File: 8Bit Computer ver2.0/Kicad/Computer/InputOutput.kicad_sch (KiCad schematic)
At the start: 147 parts, among them IC102 SN74LVC1G32DBVR, IC236 SN74F521DWR, IC237 SN74F521DWR, IC238 DS1100Z-150+, IC239 SN74LVC1G14DBVR, IC240 SN74LVC1G86DBVR, IC241 SN74LVC1G14DBVR, IC242 SN74F521DWR, IC243 SN74F521DWR, IC244 SN74LVC1G14DBVR, IC245 SN74LVC1G14DBVR, IC246 SN74LVC1G14DBVR, IC247 SN74ABT574ADWR, IC248 SN74LVC1G14DBVR, IC249 SN74LVC1G14DBVR, IC250 SN74AHC74DR, IC251 SN74LVC1G08DBVR, IC252 SN74LVC1G14DBVR, IC253 SN74AHC74DR, IC254 SN74AHC74DR, IC255 SN74ABT574ADWR, IC256 SN74ABT245BDWR, IC257 SN74AHC74DR, IC258 SN74LVC1G08DBVR, IC259 SN74ABT245BDWR, IC260 SN74ABT245BDWR, IC261 MP2338GTL-Z, IC262 SN74AHC540DWR, IC263 SN74AHC540DWR, IC272 SN74F521DWR, IC273 SN74LVC1G14DBVR

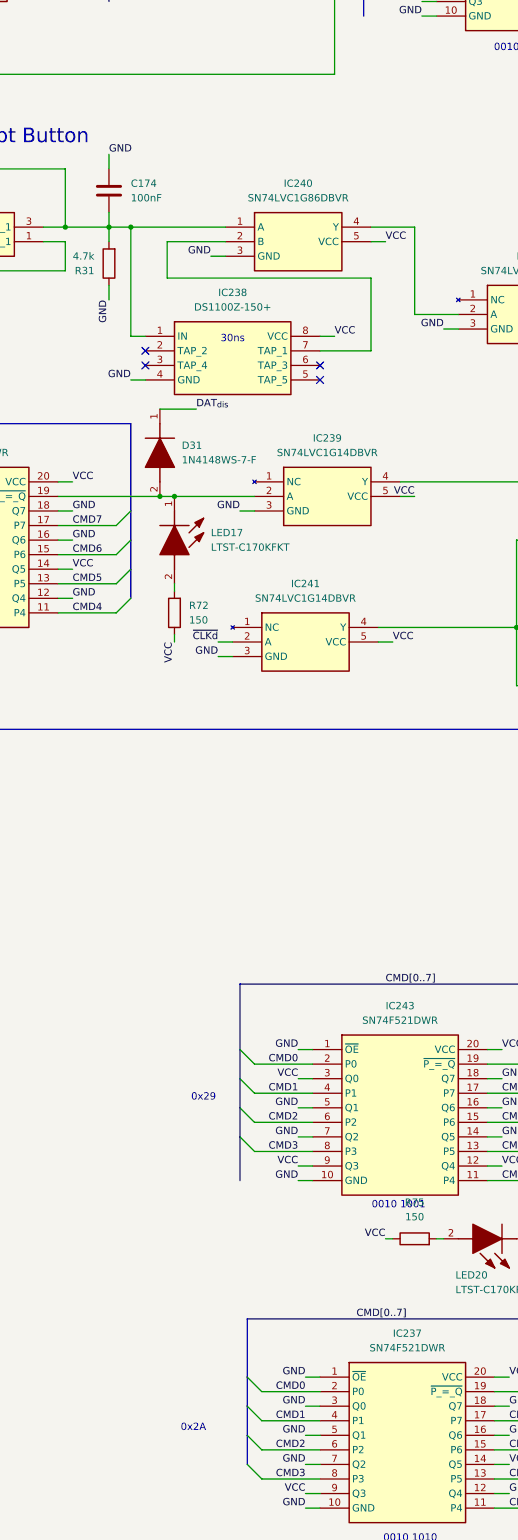
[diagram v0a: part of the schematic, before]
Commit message: updated T76 software, Kicad bugs
changed the inverting outs of IC199 to non inverting
changed Pin of CMD decoder IC237 0x2A from GND to VCC (pin5)
deleted diode d30
changed silkscreen of the Clock gen mux from 0 1 555 to 1 0 555 and buttonclk from 1 0 to 0 1
changed the DS1100-150+ of the edge detector to an or gate SN74HCS32
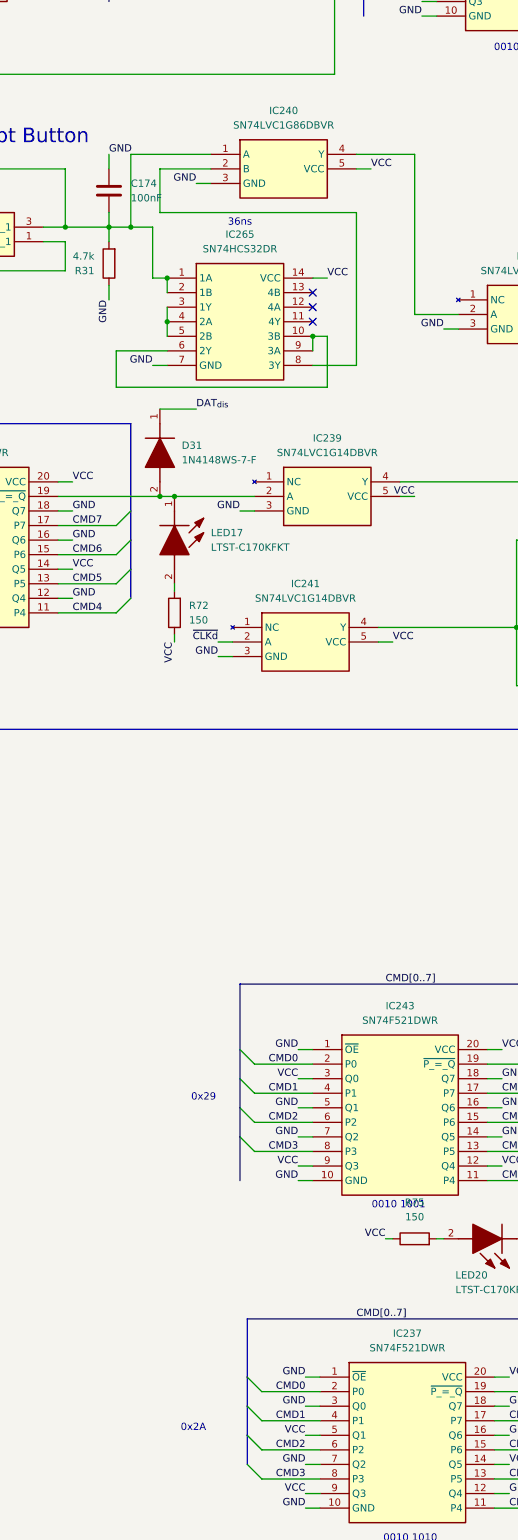
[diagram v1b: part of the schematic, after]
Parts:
- removed IC238: DS1100Z-150+, Samacsys:SOIC127P600X175-8N, symbol Samacsys:DS1100Z-150+
- added IC265: SN74HCS32DR, Samacsys:SOIC127P600X175-14N, symbol Samacsys:SN74HCS32DR
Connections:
- net GND: now also IC265.7 (GND); no longer IC237.5 (Q1)
- net VCC: now also IC237.5 (Q1), IC265.14 (VCC)
- net at C174.1, IC102.2 (B), IC240.1 (A)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: now also IC265.1 (1A), IC265.2 (1B)
- net at IC240.2 (B): now also IC265.8 (3Y)
- new net: IC265.10 (3B), IC265.6 (2Y), IC265.9 (3A)
- new net: IC265.3 (1Y), IC265.4 (2A), IC265.5 (2B)
- no-connect marks 14 -> 13
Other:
- note added: "36ns"
- note removed: "30ns"
- moved on the sheet: IC240

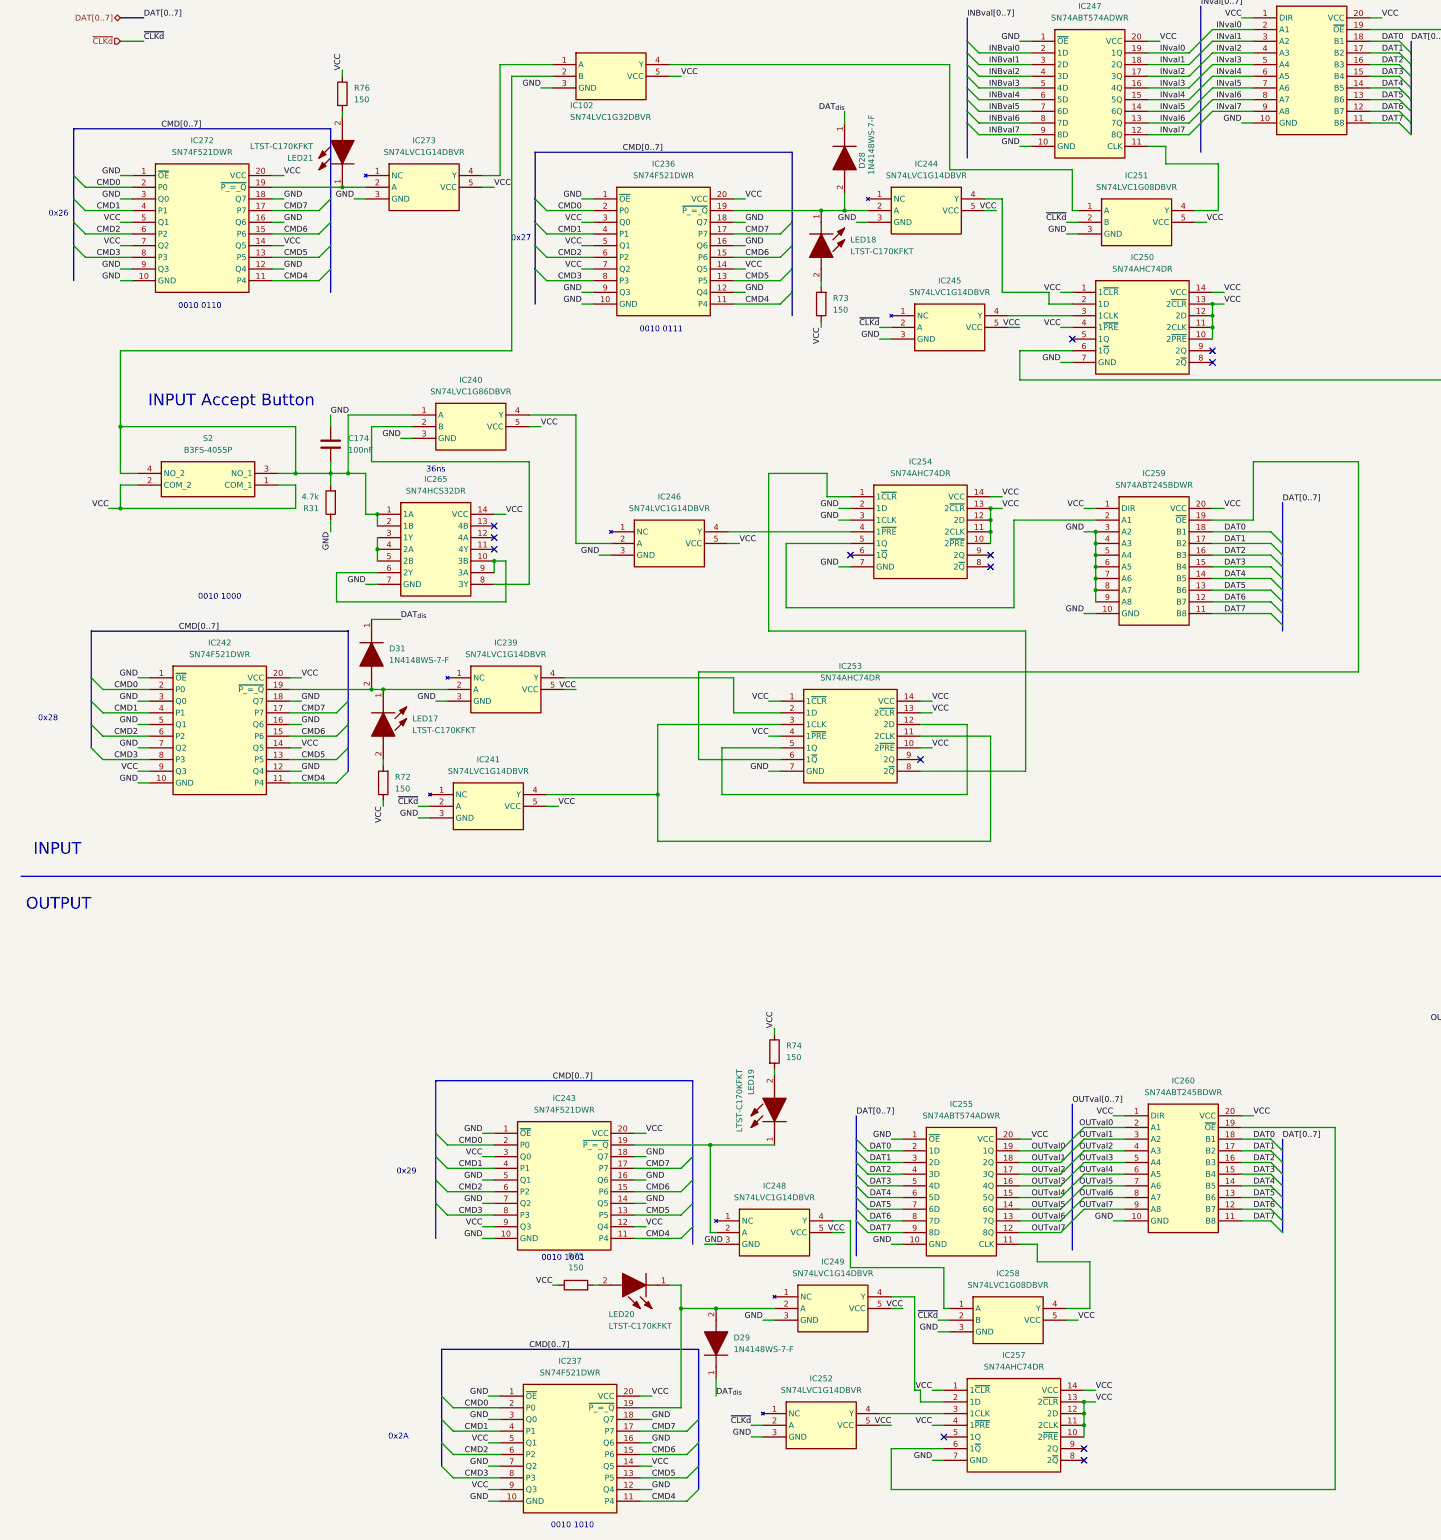
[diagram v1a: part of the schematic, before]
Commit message: Kicad
fixed some design errors(dat dis DistShiftreg, wrong cmd pins)
added description to every CMD for better debug, use CTRL+f and use option "Whole words only" to search e.g. inc
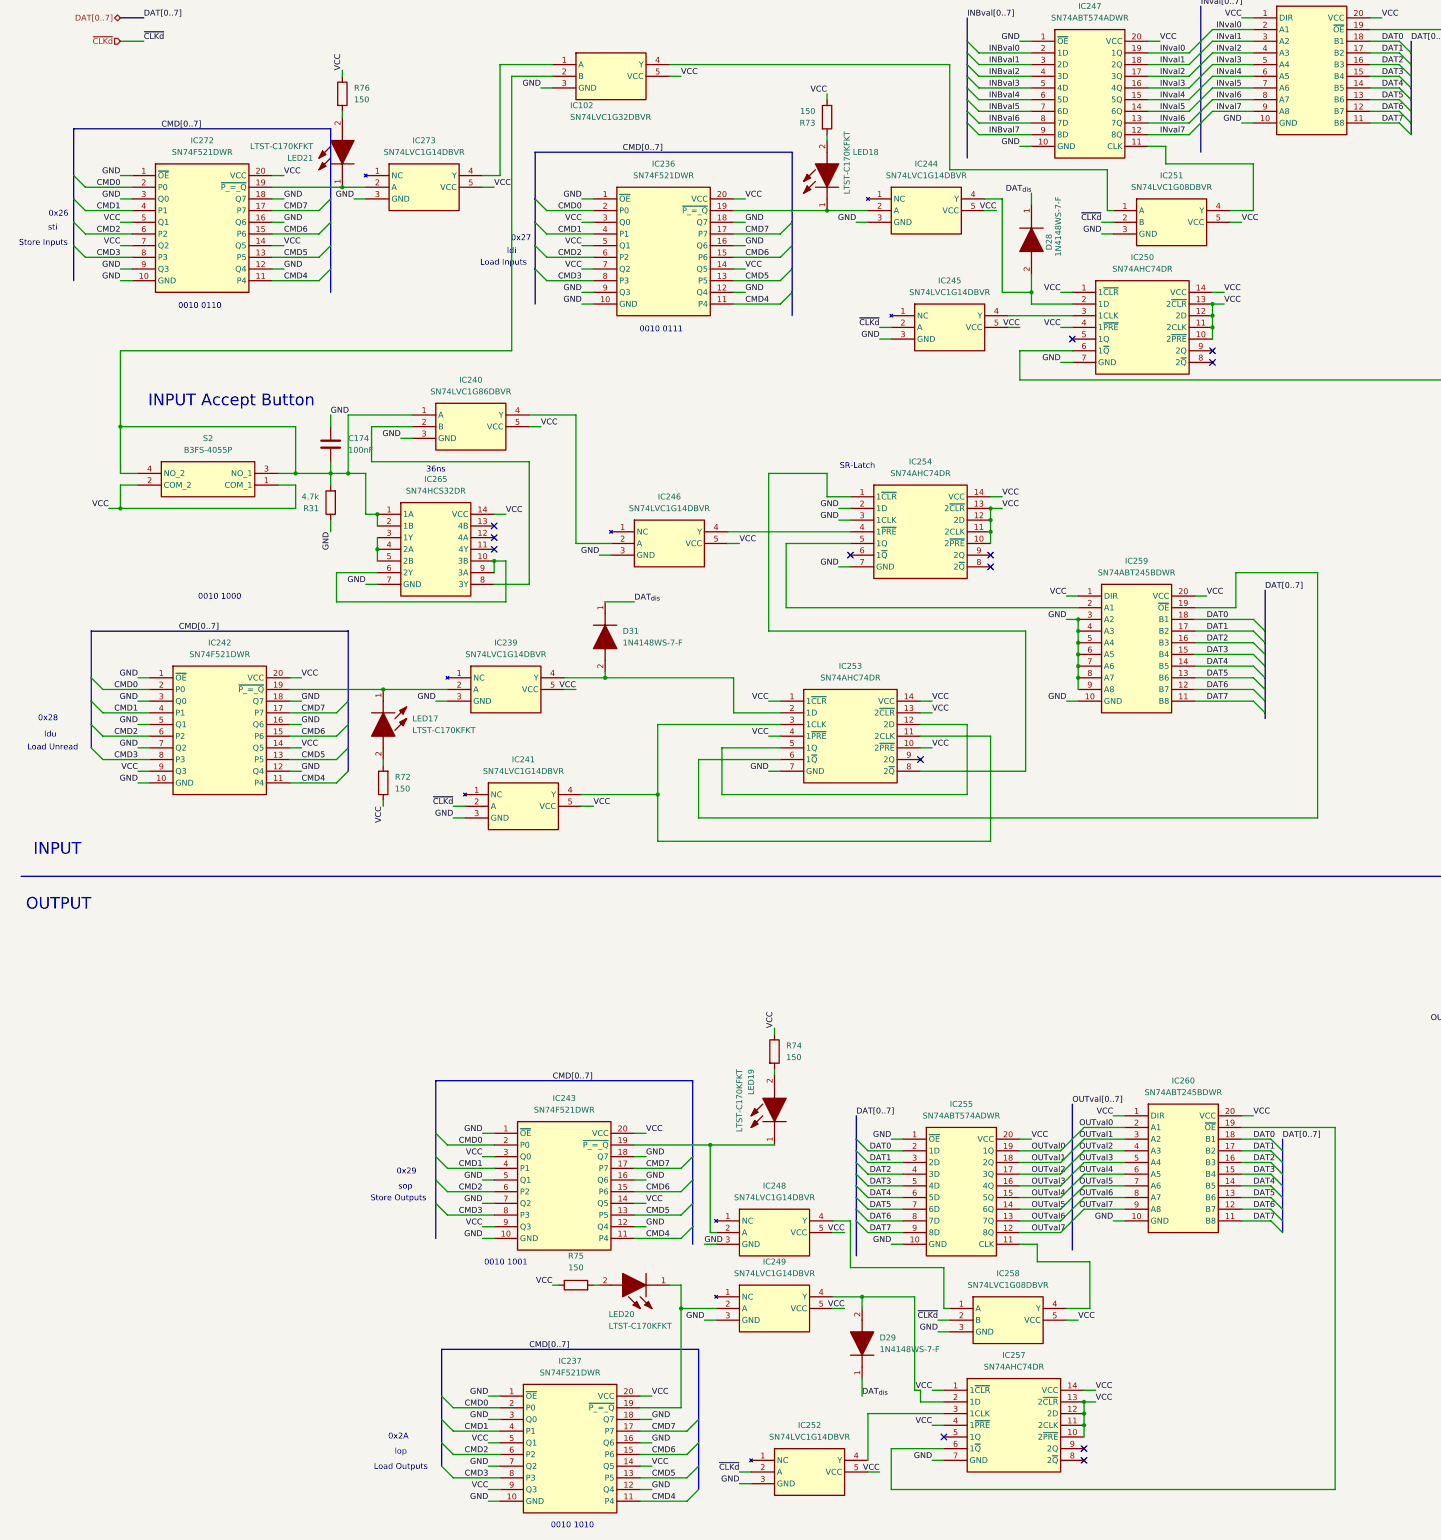
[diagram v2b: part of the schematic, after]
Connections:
- net GND: now also IC243.12 (Q4); no longer IC243.14 (Q5)
- net VCC: now also IC243.14 (Q5); no longer IC243.12 (Q4)
- net at IC244.4 (Y), IC250.2 (1D): now also D28.2 (A)
- net at IC237.19 (~{P_=_Q}), IC249.2 (A), LED20.1 (K): no longer D29.2 (A)
- net at IC236.19 (~{P_=_Q}), IC244.2 (A), LED18.1 (K): no longer D28.2 (A)
- net at IC239.2 (A), IC242.19 (~{P_=_Q}), LED17.1 (K): no longer D31.2 (A)
- net at IC249.4 (Y), IC257.2 (1D): now also D29.2 (A)
- net at IC239.4 (Y), IC253.2 (1D): now also D31.2 (A)
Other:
- note added: "Load Inputs"
- note added: "Load Outputs"
- note added: "Load Unread"
- note added: "SR-Latch"
- note added: "Store Inputs"
- note added: "Store Outputs"
- note added: "ldi"
- note added: "ldu"
- note added: "lop"
- note added: "sop"
- note added: "sti"
- moved on the sheet: D28, D29, D31, IC241, IC249, IC251, IC252, IC259, LED18, R73

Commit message: changed page numbers, every schematic is now A4
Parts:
- removed C181, C183, C184, C185, C186, C187, C188, C189: 100nF, Capacitor_SMD:C_1206_3216Metric_Pad1.33x1.80mm_HandSolder, symbol Device:C
- removed D28, D29, D31: 1N4148WS-7-F, Samacsys:SOD2513X120N, symbol Samacsys:1N4148WS-7-F
- removed IC102: SN74LVC1G32DBVR, Samacsys:SOT95P280X145-5N, symbol Samacsys:SN74LVC1G32DBVR
- removed IC236, IC237, IC242, IC243, IC272: SN74F521DWR, Samacsys:SOIC127P1030X265-20N, symbol Samacsys:SN74F521DWR
- removed IC239, IC241, IC244, IC245, IC246, IC248, IC249, IC252, IC273: SN74LVC1G14DBVR, Samacsys:SOT95P280X145-5N, symbol Samacsys:SN74LVC1G14DBVR
- removed IC240: SN74LVC1G86DBVR, Samacsys:SOT95P280X145-5N, symbol Samacsys:SN74LVC1G86DBVR
- removed IC247, IC255: SN74ABT574ADWR, Samacsys:SOIC127P1030X265-20N, symbol Samacsys:SN74ABT574ADWR
- removed IC250, IC253, IC254, IC257: SN74AHC74DR, Samacsys:SOIC127P600X175-14N, symbol Samacsys:SN74AHC74DR
- removed IC251, IC258: SN74LVC1G08DBVR, Samacsys:SOT95P280X145-5N, symbol Samacsys:SN74LVC1G08DBVR
- removed IC256, IC259, IC260: SN74ABT245BDWR, Samacsys:SOIC127P1030X265-20N, symbol Samacsys:SN74ABT245BDWR
- removed IC262, IC263: SN74AHC540DWR, Samacsys:SOIC127P1030X265-20N, symbol Samacsys:SN74AHC540DWR
- removed IC265: SN74HCS32DR, Samacsys:SOIC127P600X175-14N, symbol Samacsys:SN74HCS32DR
- removed LED1, LED10, LED12, LED2, LED3, LED4, LED6, LED8: LTST-C170KRKT, Samacsys:LEDC2012X120N, symbol Samacsys:LTST-C170KRKT
- removed LED11, LED13, LED14, LED15, LED16, LED5, LED7, LED9: LTST-C171TBKT, Samacsys:LTSTC171TBKT, symbol Samacsys:LTST-C171TBKT
- removed LED17, LED18, LED19, LED20, LED21: LTST-C170KFKT, Samacsys:LEDC2012X120N, symbol Samacsys:LTST-C170KFKT
- removed R35, R39, R42, R45, R50, R54, R57, R60: 4.7k, Resistor_SMD:R_1206_3216Metric_Pad1.30x1.75mm_HandSolder, symbol Device:R
- removed R40, R41, R43, R44, R47, R49, R52, R55: 390, Resistor_SMD:R_1206_3216Metric_Pad1.30x1.75mm_HandSolder, symbol Device:R
- removed R46, R48, R51, R53, R56, R58, R59, R61: 270, Resistor_SMD:R_1206_3216Metric_Pad1.30x1.75mm_HandSolder, symbol Device:R
- removed R72, R73, R74, R75, R76: 150, Resistor_SMD:R_1206_3216Metric_Pad1.30x1.75mm_HandSolder, symbol Device:R
- removed S10, S3, S4, S5, S6, S7, S8, S9: 2MS1T2B3M2QES, Samacsys:2MS1T2B3M2QES, symbol Samacsys:2MS1T2B3M2QES
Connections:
- net INPUT_Acc_But: now reaches C174.1, R31.2, S2.3 (NO_1), S2.4 (NO_2)
- no-connect marks 13 -> 0
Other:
- added sheet Input_Buttons_LEDs_IO (Input_Buttons_LEDs_IO.kicad_sch)
- added sheet Input_store_IO (Input_store_IO.kicad_sch)
- added sheet Input_unread_IO (Input_unread_IO.kicad_sch)
- added sheet Output_IO (Output_IO.kicad_sch)
- note removed: "0010 0110"
- note removed: "0010 0111"
- note removed: "0010 1000"
- note removed: "0010 1001"
- note removed: "0010 1010"
- note removed: "0x26"
- note removed: "0x27"
- note removed: "0x28"
- note removed: "0x29"
- note removed: "0x2A"
- note removed: "36ns"
- note removed: "INPUT"
- note removed: "Load Inputs"
- note removed: "Load Outputs"
- note removed: "Load Unread"
- note removed: "OUTPUT"
- note removed: "SR-Latch"
- note removed: "Store Inputs"
- note removed: "Store Outputs"
- note removed: "Switches"
- note removed: "ldi"
- note removed: "ldu"
- note removed: "lop"
- note removed: "sop"
- note removed: "sti"
- title: (none) -> ${SHEETNAME}
- moved on the sheet: C174, C175, C176, C177, C178, C179, C180, C182, C190, C191, C192, C193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
